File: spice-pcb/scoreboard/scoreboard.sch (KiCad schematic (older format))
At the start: 8 parts, among them P1 CONN_8, P2 CONN_2

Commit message: Complete 1st Draft of scoreboard, ready for shipping.
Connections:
- net VCC is gone; now on net SCLR_BAR: AFF1.3 (C.A.), AFF1.8 (C.A.), AFF2.3 (C.A.), AFF2.8 (C.A.), P1.1 (P1), WES1.16 (VCC), WES2.16 (VCC)
- net GND: now also WES1.13 (OE_BAR), WES2.13 (OE_BAR)
- net SCLR_BAR: no longer P1.6 (P6)
- removed net OE_BAR: P1.7 (P7), WES1.13 (OE_BAR), WES2.13 (OE_BAR)
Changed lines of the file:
@@
-EESchema Schematic File Version 2  date Wed 18 Jun 2014 09:06:52 AM PDT
+EESchema Schematic File Version 2  date Thu 19 Jun 2014 10:26:47 AM PDT
 LIBS:power
 LIBS:device
@@
 Sheet 1 1
 Title ""
-Date "18 jun 2014"
+Date "19 jun 2014"
 Rev ""
 Comp ""
@@
 $EndDescr
 Wire Wire Line
+	4250 5250 4450 5250
+Wire Wire Line
 	3300 4100 3550 4100
 Wire Wire Line
@@
 Wire Wire Line
 	1200 2600 1800 2600
+Wire Wire Line
+	4250 5100 4450 5100
+Text GLabel 4450 5250 2    60   Input ~ 0
+VCC
+Text GLabel 4450 5100 2    60   Input ~ 0
+GND
 $Comp
 L R_PACK8 RP2
@@
 	1    0    0    -1
 $EndComp
-Text GLabel 3200 5750 0    60   Input ~ 0
+Text GLabel 4250 5100 0    60   Input ~ 0
 OE_BAR
-Text GLabel 3200 5650 0    60   Input ~ 0
+Text GLabel 4250 5250 0    60   Input ~ 0
 SCLR_BAR
 Text GLabel 3200 5450 0    60   Input ~ 0

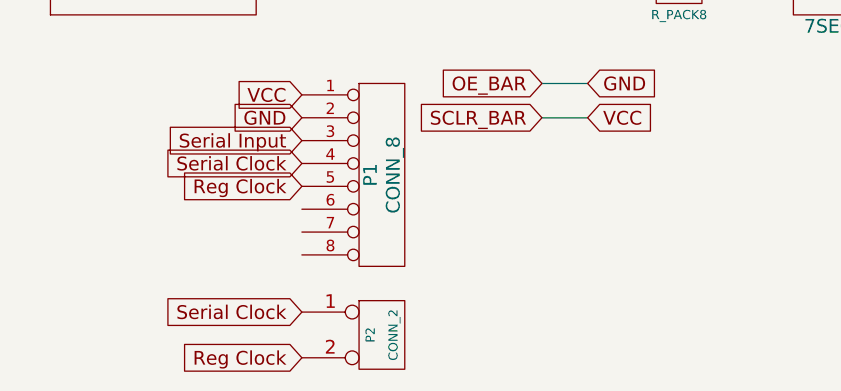
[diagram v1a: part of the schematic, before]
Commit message: Speaker added, completed version submitted for order.
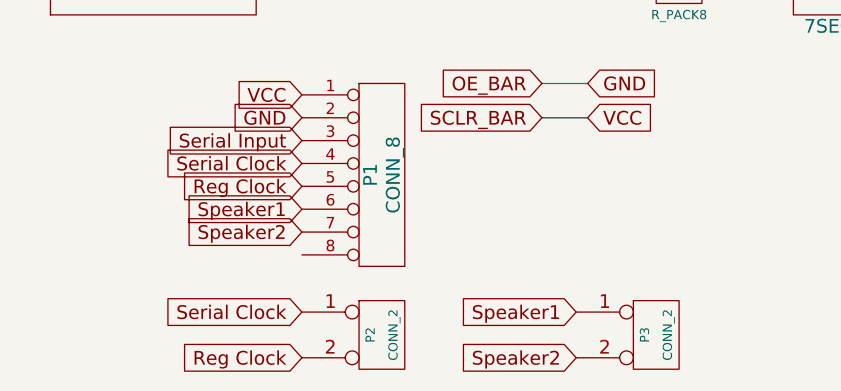
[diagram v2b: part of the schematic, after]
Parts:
- added P3: CONN_2, symbol CONN_2
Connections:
- net Speaker1: now reaches P1.6 (P6)
- net Speaker1: now also P3.1 (P1)
- net Speaker2: now reaches P1.7 (P7)
- net Speaker2: now also P3.2 (PM)
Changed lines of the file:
@@
-EESchema Schematic File Version 2  date Thu 19 Jun 2014 10:26:47 AM PDT
+EESchema Schematic File Version 2  date Thu 19 Jun 2014 09:07:59 AM PDT
 LIBS:power
 LIBS:device
@@
 Comment4 ""
 $EndDescr
+Text GLabel 4400 6300 0    60   Input ~ 0
+Speaker2
+Text GLabel 4400 6100 0    60   Input ~ 0
+Speaker1
+Text GLabel 3200 5750 0    60   Input ~ 0
+Speaker2
+Text GLabel 3200 5650 0    60   Input ~ 0
+Speaker1
+$Comp
+L CONN_2 P3
+U 1 1 53A30A7E
+P 4750 6200
+F 0 "P3" V 4700 6200 40  0000 C CNN
+F 1 "CONN_2" V 4800 6200 40  0000 C CNN
+	1    4750 6200
+	1    0    0    -1
+$EndComp
 Wire Wire Line
 	4250 5250 4450 5250
